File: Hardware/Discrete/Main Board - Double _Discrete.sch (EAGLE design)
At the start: 85 parts, among them J1 MICROMOD-2222-C, J10 MICRO-SD-PUSH-PUSH-EXT-PIN, J2 Vertical Qwiic Connector, J4 QWIIC_RIGHT_ANGLE, J5 CORTEX_JTAG_DEBUG_MINIMUM_PTH, J6 MICROMOD_FUNCTION_MAIN, J7 MICROMOD_FUNCTION_MAIN, Q1 3.1A/30V/105mΩ, U1 SN74HCS4075PWR, U2 MCP73831, U3 ESD Diode, U4 AP7347DQ-33W5-7K-3.3V, U5 AP7361C-33, U6 74HC2G04GV, U7 SN74HCS11PWR, U8 SN74HCS4075PWR

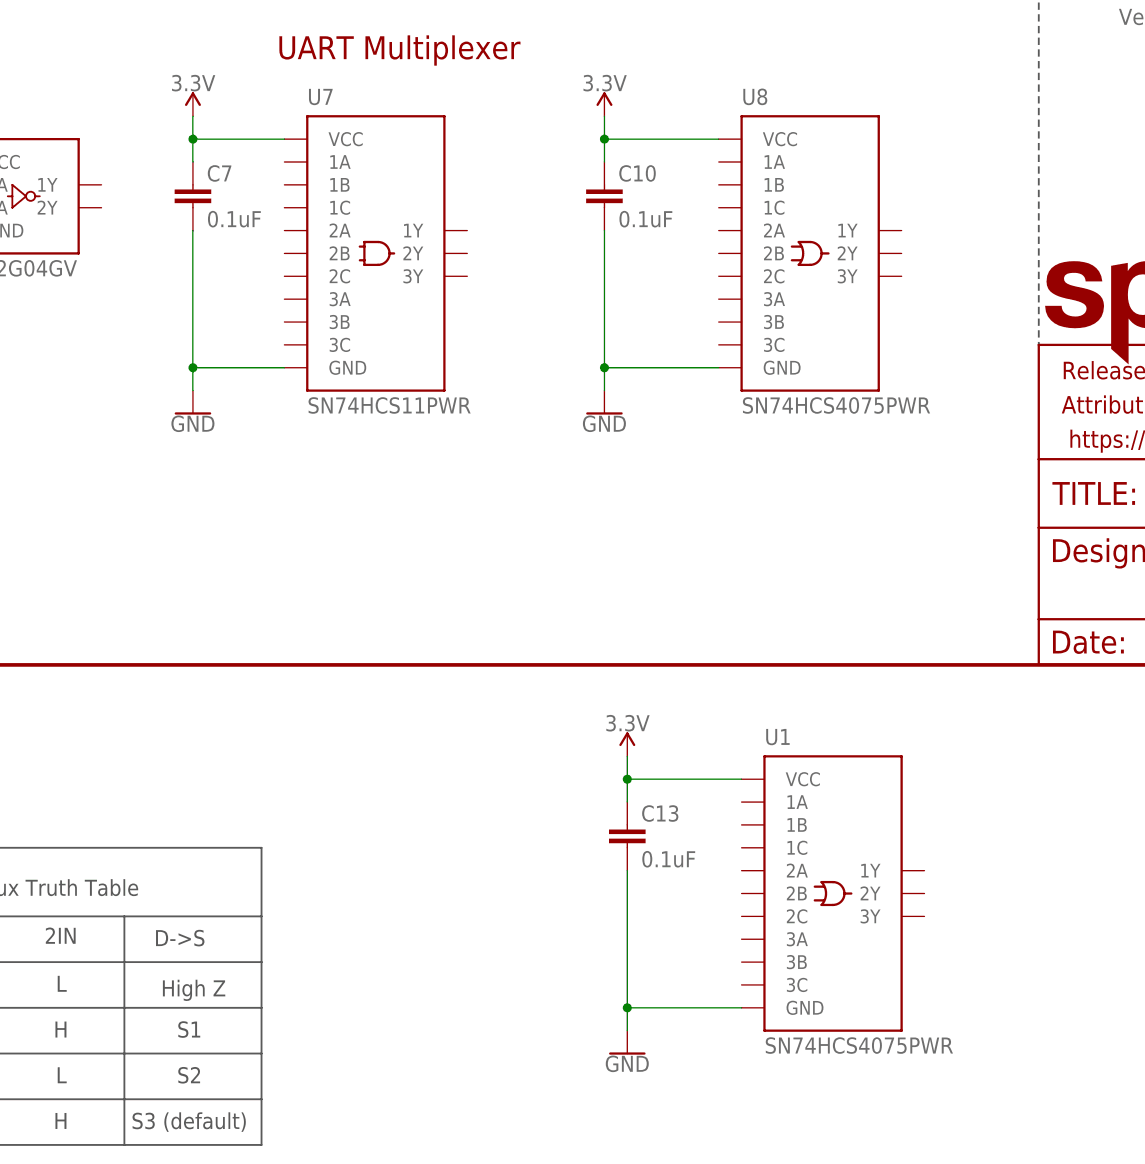
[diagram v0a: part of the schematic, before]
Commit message: Matches length of D+ and D-
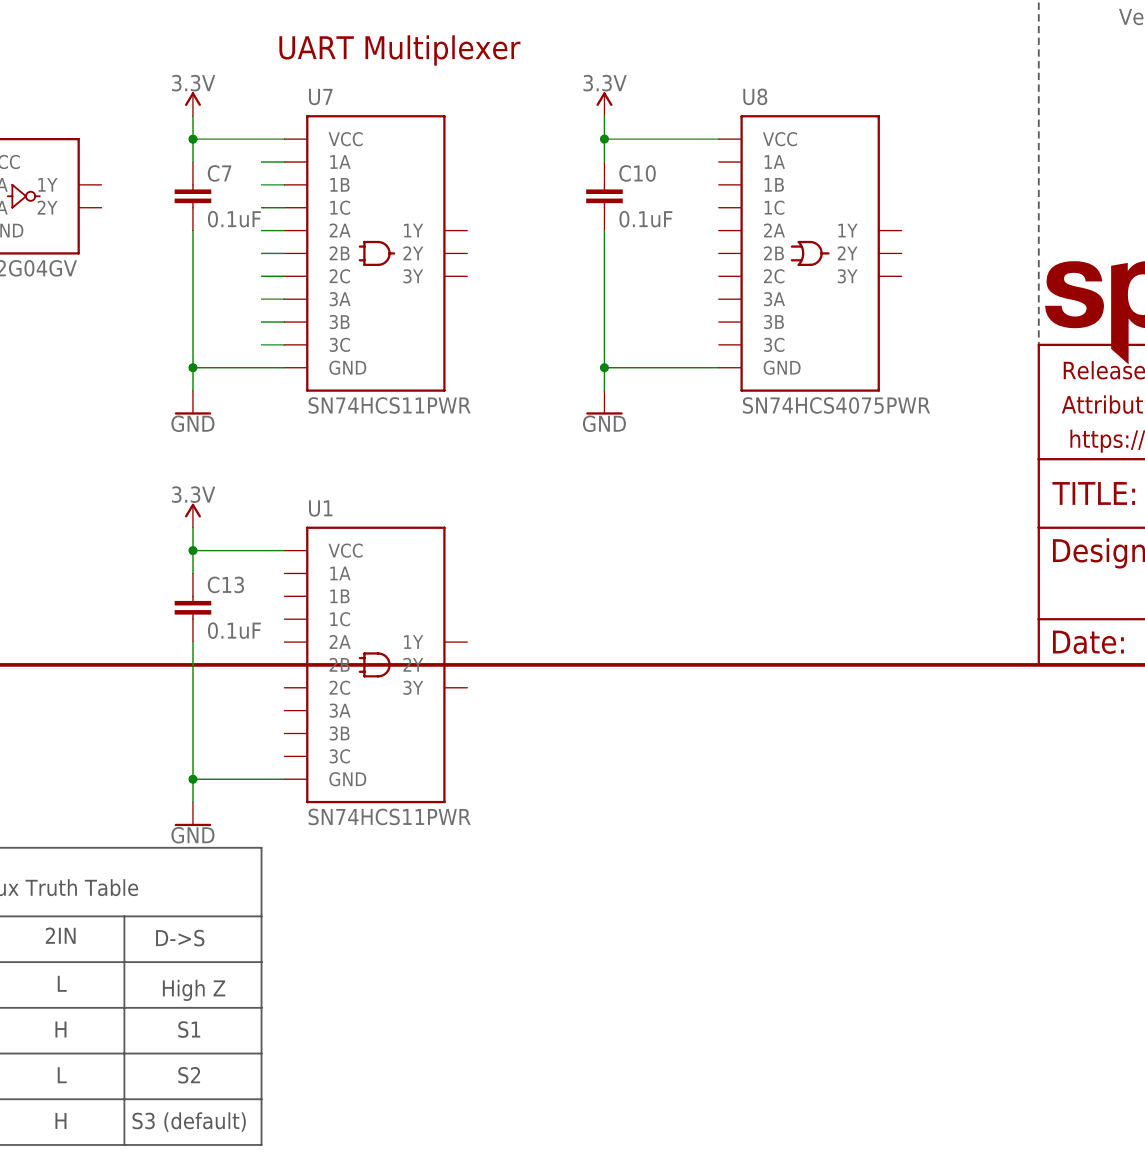
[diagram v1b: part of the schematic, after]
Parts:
- U1: value SN74HCS4075PWR -> SN74HCS11PWR; device dip_switch:SN74HCS4075PWR -> dip_switch:SN74HCS11PWR
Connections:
- new net N$16: U7.1B
- new net N$17: U7.1C
- new net N$18: U7.2A
- new net N$19: U7.2B
- new net N$20: U7.2C
- new net N$21: U7.3A
- new net N$22: U7.3B
- new net N$23: U7.3C
- new net N$9: U7.1A
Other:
- moved on the sheet: C13
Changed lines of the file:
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@@
 <part name="SUPPLY35" library="SparkFun-PowerSymbols" deviceset="3.3V" device=""/>
 <part name="SUPPLY36" library="SparkFun-PowerSymbols" deviceset="3.3V" device=""/>
-<part name="U1" library="dip_switch" deviceset="SN74HCS4075PWR" device=""/>
+<part name="U1" library="dip_switch" deviceset="SN74HCS11PWR" device=""/>
 <part name="C13" library="SparkFun-Capacitors" deviceset="0.1UF" device="-0603-25V-(+80/-20%)" value="0.1uF"/>
 <part name="GND18" library="SparkFun-PowerSymbols" deviceset="GND" device=""/>
@@
 <attribute name="VALUE" x="281.94" y="63.754" size="1.778" layer="96" font="vector" align="bottom-center"/>
 </instance>
-<instance part="U1" gate="G$1" x="317.5" y="-30.48" smashed="yes">
-<attribute name="NAME" x="299.72" y="-8.89" size="1.778" layer="95" font="vector"/>
-<attribute name="VALUE" x="299.72" y="-43.18" size="1.778" layer="95" font="vector"/>
-</instance>
-<instance part="C13" gate="G$1" x="284.48" y="-20.32" smashed="yes">
-<attribute name="NAME" x="286.004" y="-17.399" size="1.778" layer="95" font="vector"/>
-<attribute name="VALUE" x="286.004" y="-22.479" size="1.778" layer="96" font="vector"/>
-</instance>
-<instance part="GND18" gate="1" x="284.48" y="-43.18" smashed="yes">
-<attribute name="VALUE" x="284.48" y="-43.434" size="1.778" layer="96" font="vector" align="top-center"/>
-</instance>
-<instance part="SUPPLY18" gate="G$1" x="284.48" y="-10.16" smashed="yes">
-<attribute name="VALUE" x="284.48" y="-7.366" size="1.778" layer="96" font="vector" align="bottom-center"/>
+<instance part="U1" gate="G$1" x="266.7" y="-5.08" smashed="yes">
+<attribute name="NAME" x="248.92" y="16.51" size="1.778" layer="95" font="vector"/>
+<attribute name="VALUE" x="248.92" y="-17.78" size="1.778" layer="95" font="vector"/>
+</instance>
+<instance part="C13" gate="G$1" x="236.22" y="5.08" smashed="yes">
+<attribute name="NAME" x="237.744" y="8.001" size="1.778" layer="95" font="vector"/>
+<attribute name="VALUE" x="237.744" y="2.921" size="1.778" layer="96" font="vector"/>
+</instance>
+<instance part="GND18" gate="1" x="236.22" y="-17.78" smashed="yes">
+<attribute name="VALUE" x="236.22" y="-18.034" size="1.778" layer="96" font="vector" align="top-center"/>
+</instance>
+<instance part="SUPPLY18" gate="G$1" x="236.22" y="15.24" smashed="yes">
+<attribute name="VALUE" x="236.22" y="18.034" size="1.778" layer="96" font="vector" align="bottom-center"/>
 </instance>
 </instances>
@@
 <segment>
 <pinref part="U1" gate="G$1" pin="VCC"/>
-<wire x1="297.18" y1="-12.7" x2="284.48" y2="-12.7" width="0.1524" layer="91"/>
+<wire x1="246.38" y1="12.7" x2="236.22" y2="12.7" width="0.1524" layer="91"/>
 <pinref part="C13" gate="G$1" pin="1"/>
-<wire x1="284.48" y1="-12.7" x2="284.48" y2="-15.24" width="0.1524" layer="91"/>
-<wire x1="284.48" y1="-12.7" x2="284.48" y2="-10.16" width="0.1524" layer="91"/>
-<junction x="284.48" y="-12.7"/>
+<wire x1="236.22" y1="10.16" x2="236.22" y2="12.7" width="0.1524" layer="91"/>
+<wire x1="236.22" y1="12.7" x2="236.22" y2="15.24" width="0.1524" layer="91"/>
+<junction x="236.22" y="12.7"/>
 <pinref part="SUPPLY18" gate="G$1" pin="3.3V"/>
 </segment>
@@
 <segment>
 <pinref part="U1" gate="G$1" pin="GND"/>
-<wire x1="297.18" y1="-38.1" x2="284.48" y2="-38.1" width="0.1524" layer="91"/>
-<wire x1="284.48" y1="-38.1" x2="284.48" y2="-40.64" width="0.1524" layer="91"/>
+<wire x1="246.38" y1="-12.7" x2="236.22" y2="-12.7" width="0.1524" layer="91"/>
+<wire x1="236.22" y1="-12.7" x2="236.22" y2="-15.24" width="0.1524" layer="91"/>
 <pinref part="GND18" gate="1" pin="GND"/>
 <pinref part="C13" gate="G$1" pin="2"/>
-<wire x1="284.48" y1="-22.86" x2="284.48" y2="-38.1" width="0.1524" layer="91"/>
-<junction x="284.48" y="-38.1"/>
+<wire x1="236.22" y1="2.54" x2="236.22" y2="-12.7" width="0.1524" layer="91"/>
+<junction x="236.22" y="-12.7"/>
 </segment>
 </net>
@@
 </segment>
 </net>
+<net name="N$9" class="0">
+<segment>
+<pinref part="U7" gate="G$1" pin="1A"/>
+<wire x1="243.84" y1="55.88" x2="246.38" y2="55.88" width="0.1524" layer="91"/>
+</segment>
+</net>
+<net name="N$16" class="0">
+<segment>
+<pinref part="U7" gate="G$1" pin="1B"/>
+<wire x1="243.84" y1="53.34" x2="246.38" y2="53.34" width="0.1524" layer="91"/>
+</segment>
+</net>
+<net name="N$17" class="0">
+<segment>
+<pinref part="U7" gate="G$1" pin="1C"/>
+<wire x1="243.84" y1="50.8" x2="246.38" y2="50.8" width="0.1524" layer="91"/>
+</segment>
+</net>
+<net name="N$18" class="0">
+<segment>
+<pinref part="U7" gate="G$1" pin="2A"/>
+<wire x1="243.84" y1="48.26" x2="246.38" y2="48.26" width="0.1524" layer="91"/>
+</segment>
+</net>
+<net name="N$19" class="0">
+<segment>
+<pinref part="U7" gate="G$1" pin="2B"/>
+<wire x1="243.84" y1="45.72" x2="246.38" y2="45.72" width="0.1524" layer="91"/>
+</segment>
+</net>
+<net name="N$20" class="0">
+<segment>
+<pinref part="U7" gate="G$1" pin="2C"/>
+<wire x1="243.84" y1="43.18" x2="246.38" y2="43.18" width="0.1524" layer="91"/>
+</segment>
+</net>
+<net name="N$21" class="0">
+<segment>
+<pinref part="U7" gate="G$1" pin="3A"/>
+<wire x1="243.84" y1="40.64" x2="246.38" y2="40.64" width="0.1524" layer="91"/>
+</segment>
+</net>
+<net name="N$22" class="0">
+<segment>
+<pinref part="U7" gate="G$1" pin="3B"/>
+<wire x1="243.84" y1="38.1" x2="246.38" y2="38.1" width="0.1524" layer="91"/>
+</segment>
+</net>
+<net name="N$23" class="0">
+<segment>
+<pinref part="U7" gate="G$1" pin="3C"/>
+<wire x1="243.84" y1="35.56" x2="246.38" y2="35.56" width="0.1524" layer="91"/>
+</segment>
+</net>
